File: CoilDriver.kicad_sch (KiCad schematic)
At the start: 27 parts, among them Q1 IRLML2803, Q2 SiRA99DP, U2 DRV8235RTER

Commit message: v3.1 Updates
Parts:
- removed R48, R50: 0R, Resistor_SMD:R_0603_1608Metric, symbol Device:R_Small
- C37: renamed from C26; value 10uF -> 10u; symbol Device:C -> Device:C_Small
- C38: renamed from C27; value 0.1uF -> 100n; symbol Device:C -> Device:C_Small
- C41: renamed from C22; value 1nF -> 1n; symbol Device:C -> Device:C_Small
- C42: renamed from C28; value 0.1uF -> 100n; symbol Device:C -> Device:C_Small
- R68: renamed from R33; symbol Device:R -> Device:R_Small
- R86: renamed from R49; now not fitted
- R87: renamed from R51; now not fitted
- R88: renamed from R32; symbol Device:R -> Device:R_Small
- R89: renamed from R52; symbol Device:R -> Device:R_Small
- R90: renamed from R53; symbol Device:R -> Device:R_Small
- renumbered F2 to F10, Q2 to Q16, Q1 to Q17, R36 to R64, R37 to R65, R39 to R66, R38 to R67, R54 to R69, R28 to R82, R29 to R83, R30 to R84, R31 to R85, U2 to U9
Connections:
- net PERI_3V3 is gone; now on net 3V3_P: R69.2
- net A0_COIL renamed A0
- net A1_COIL renamed A1
- net MAIN_3V3 renamed 3V3_P
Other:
- sheet I2C Single Protection renamed I2C Single Protection4
- sheet I2C Single Protection1 renamed I2C Single Protection5
- note added: "#TODO: Spec Resistors"
- company: (none) -> Carnegie Mellon University
- title: (none) -> Argus XY Solar Panel
- moved on the sheet: C37, C41, C42, D10, D9, F10, Q16, Q17, R64, R65, R66, R67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

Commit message: Local Stash
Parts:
- R64: value 2.7k -> 2k7
- R69: symbol SolarPanels:R_Small -> Device:R_Small
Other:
- moved on the sheet: C42, R66, R90
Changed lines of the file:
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@@
 	(wire
 		(pts
-			(xy 205.74 137.16) (xy 205.74 140.97)
+			(xy 205.74 137.16) (xy 205.74 139.7)
 		)
 		(stroke
@@
 	(wire
 		(pts
-			(xy 222.25 146.05) (xy 222.25 148.59)
+			(xy 222.25 144.78) (xy 222.25 147.32)
 		)
 		(stroke
@@
 	(wire
 		(pts
-			(xy 69.85 71.12) (xy 71.12 71.12)
+			(xy 68.58 71.12) (xy 71.12 71.12)
 		)
 		(stroke
@@
 	(wire
 		(pts
-			(xy 222.25 137.16) (xy 222.25 140.97)
+			(xy 222.25 137.16) (xy 222.25 139.7)
 		)
 		(stroke
@@
 	(wire
 		(pts
-			(xy 205.74 146.05) (xy 205.74 148.59)
+			(xy 205.74 144.78) (xy 205.74 147.32)
 		)
 		(stroke
@@
 	(wire
 		(pts
-			(xy 63.5 71.12) (xy 64.77 71.12)
-		)
-		(stroke
-			(width 0)
-			(type default)
-		)
-	)
-	(wire
-		(pts
 			(xy 124.46 82.55) (xy 124.46 81.28)
 		)
@@
 	)
 	(symbol
-		(lib_name "R_Small_1")
 		(lib_id "Device:R_Small")
 		(at 222.25 132.08 0)
@@
 			)
 		)
-		(property "Value" "2.7k"
+		(property "Value" "2k7"
 			(at 45.72 79.248 0)
 			(effects
@@
 	(symbol
 		(lib_id "Device:C_Small")
-		(at 205.74 143.51 0)
+		(at 205.74 142.24 0)
 		(unit 1)
 		(exclude_from_sim no)
@@
 		(dnp no)
 		(property "Reference" "C42"
-			(at 208.788 142.494 0)
+			(at 208.788 141.224 0)
 			(effects
 				(font
@@
 		)
 		(property "Value" "100n"
-			(at 208.788 144.526 0)
+			(at 208.788 143.256 0)
 			(effects
 				(font
@@
 		)
 		(property "Footprint" "Capacitor_SMD:C_0603_1608Metric"
-			(at 205.74 143.51 0)
+			(at 205.74 142.24 0)
 			(effects
 				(font
@@
 		)
 		(property "Datasheet" "~"
-			(at 205.74 143.51 0)
+			(at 205.74 142.24 0)
 			(effects
 				(font
@@
 		)
 		(property "Description" "Unpolarized capacitor, small symbol"
-			(at 205.74 143.51 0)
+			(at 205.74 142.24 0)
 			(effects
 				(font
@@
 	(symbol
 		(lib_id "power:GND")
-		(at 205.74 148.59 0)
+		(at 205.74 147.32 0)
 		(unit 1)
 		(exclude_from_sim no)
@@
 		(dnp no)
 		(property "Reference" "#PWR036"
-			(at 205.74 154.94 0)
+			(at 205.74 153.67 0)
 			(effects
 				(font
@@
 		)
 		(property "Value" "GND"
-			(at 205.74 152.654 0)
+			(at 205.74 151.384 0)
 			(effects
 				(font
@@
 		)
 		(property "Footprint" ""
-			(at 205.74 148.59 0)
+			(at 205.74 147.32 0)
 			(effects
 				(font
@@
 		)
 		(property "Datasheet" ""
-			(at 205.74 148.59 0)
+			(at 205.74 147.32 0)
 			(effects
 				(font
@@
 		)
 		(property "Description" "Power symbol creates a global label with name \"GND\" , ground"
-			(at 205.74 148.59 0)
+			(at 205.74 147.32 0)
 			(effects
 				(font
@@
 	)
 	(symbol
-		(lib_id "SolarPanels:R_Small")
+		(lib_id "Device:R_Small")
 		(at 241.3 81.28 180)
 		(unit 1)
@@
 	)
 	(symbol
-		(lib_name "R_Small_2")
 		(lib_id "Device:R_Small")
 		(at 149.86 73.66 0)
@@
 	(symbol
 		(lib_id "Device:R_Small")
-		(at 67.31 71.12 90)
+		(at 66.04 71.12 90)
 		(unit 1)
 		(exclude_from_sim no)
@@
 		(dnp no)
 		(property "Reference" "R66"
-			(at 67.31 73.406 90)
+			(at 66.04 73.406 90)
 			(effects
 				(font
@@
 		)
 		(property "Value" "4k7"
-			(at 67.056 75.438 90)
+			(at 65.786 75.438 90)
 			(effects
 				(font
@@
 		)
 		(property "Footprint" "Resistor_SMD:R_0603_1608Metric"
-			(at 67.31 71.12 0)
+			(at 66.04 71.12 0)
 			(effects
 				(font
@@
 		)
 		(property "Datasheet" "~"
-			(at 67.31 71.12 0)
+			(at 66.04 71.12 0)
 			(effects
 				(font
@@
 		)
 		(property "Description" "Resistor, small symbol"
-			(at 67.31 71.12 0)
+			(at 66.04 71.12 0)
 			(effects
 				(font
@@
 			)
 		)
+		(property "Sim.Pin" "1=K 2=A"
+			(at 46.99 85.09 0)
+			(effects
+				(font
+					(size 1.27 1.27)
+				)
+				(hide yes)
+			)
+		)
 		(pin "2"
 		)
@@
 	(symbol
 		(lib_id "power:GND")
-		(at 222.25 148.59 0)
+		(at 222.25 147.32 0)
 		(unit 1)
 		(exclude_from_sim no)
@@
 		(dnp no)
 		(property "Reference" "#PWR039"
-			(at 222.25 154.94 0)
+			(at 222.25 153.67 0)
 			(effects
 				(font
@@
 		)
 		(property "Value" "GND"
-			(at 222.25 152.654 0)
+			(at 222.25 151.384 0)
 			(effects
 				(font
@@
 		)
 		(property "Footprint" ""
-			(at 222.25 148.59 0)
+			(at 222.25 147.32 0)
 			(effects
 				(font
@@
 		)
 		(property "Datasheet" ""
-			(at 222.25 148.59 0)
+			(at 222.25 147.32 0)
 			(effects
 				(font
@@
 		)
 		(property "Description" "Power symbol creates a global label with name \"GND\" , ground"
-			(at 222.25 148.59 0)
+			(at 222.25 147.32 0)
 			(effects
 				(font
@@
 	)
 	(symbol
-		(lib_name "R_Small_3")
 		(lib_id "Device:R_Small")
-		(at 222.25 143.51 0)
+		(at 222.25 142.24 0)
 		(unit 1)
 		(exclude_from_sim no)
@@
 		(dnp no)
 		(property "Reference" "R90"
-			(at 223.774 142.494 0)
+			(at 223.774 141.224 0)
 			(effects
 				(font
@@
 		)
 		(property "Value" "TBD"
-			(at 223.774 144.526 0)
+			(at 223.774 143.256 0)
 			(effects
 				(font
@@
 		)
 		(property "Footprint" "Resistor_SMD:R_0603_1608Metric"
-			(at 222.25 143.51 0)
+			(at 222.25 142.24 0)
 			(effects
 				(font
@@
 		)
 		(property "Datasheet" "~"
-			(at 222.25 143.51 0)
+			(at 222.25 142.24 0)
 			(effects
 				(font
@@
 		)
 		(property "Description" "Resistor, small symbol"
-			(at 222.25 143.51 0)
+			(at 222.25 142.24 0)
 			(effects
 				(font
@@
 	)
 	(symbol
-		(lib_name "R_Small_4")
 		(lib_id "Device:R_Small")
 		(at 167.64 137.16 0)

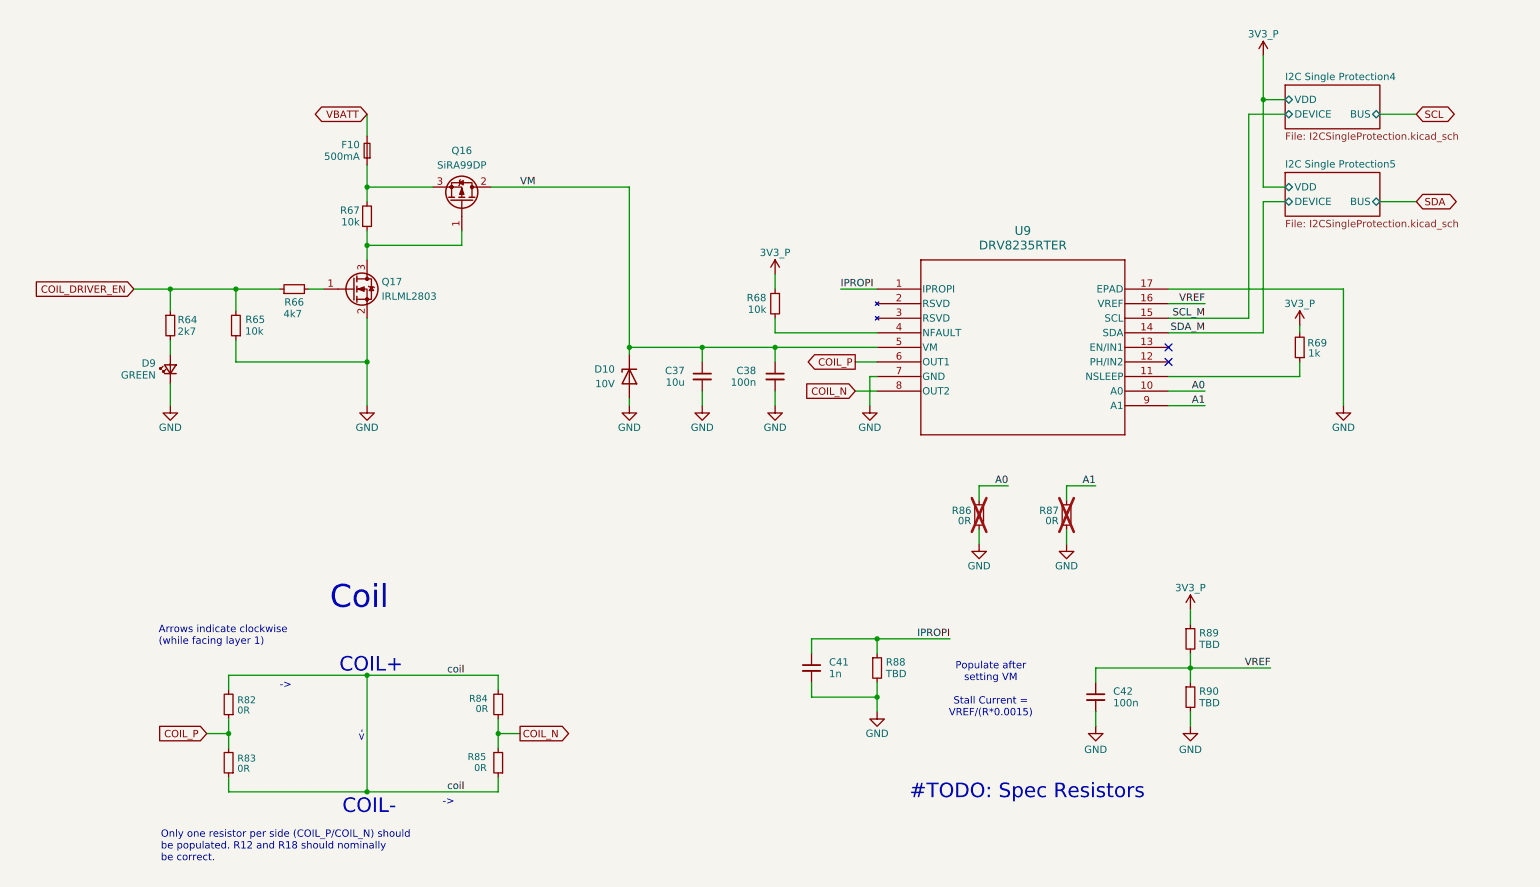
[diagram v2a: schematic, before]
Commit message: Updated access port, added deployment sensor
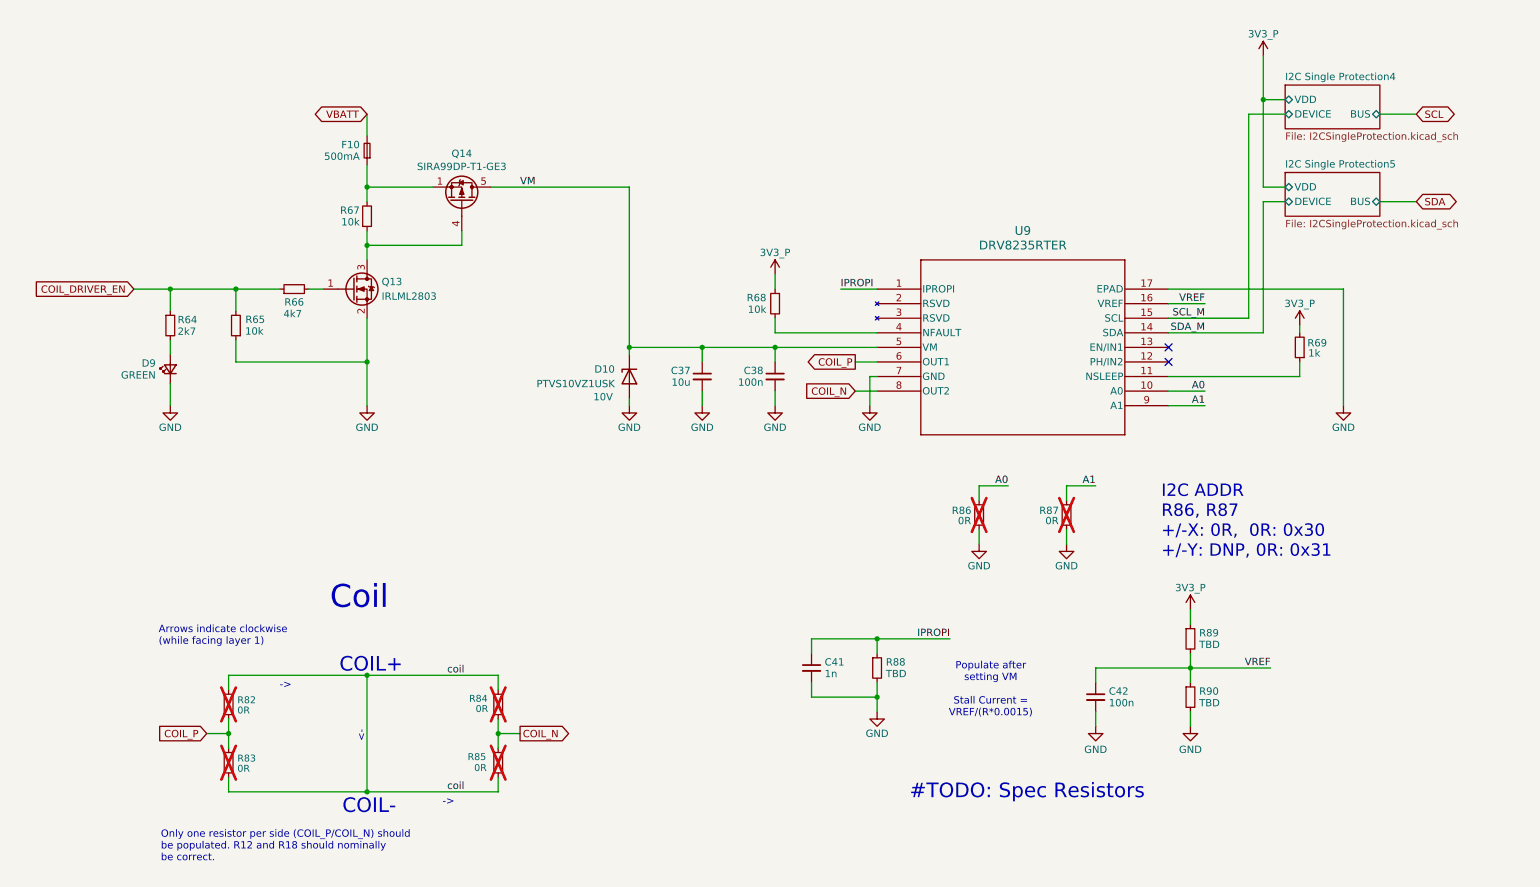
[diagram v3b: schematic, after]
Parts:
- removed Q16: SiRA99DP, Argus-Miscellaneous:PowerPAK SO-8, symbol Argus-IC:Q_PMOS_GDS
- added Q14: SIRA99DP-T1-GE3, Package_SO:PowerPAK_SO-8_Single, symbol Transistor_FET:Si7141DP
- C37: MPN (none) -> C126617
- C38, C42: MPN (none) -> C307348
- C41: MPN (none) -> C161231
- D10: value 10V -> PTVS10VZ1USK; Field5 (none) -> 10V
- D9: DIS Digi-Key -> (none); DPN 1830-1064-1-ND -> (none); MFR Inolux -> (none); MPN IN-S63AT5A -> C2909774
- Q13: renamed from Q17; MPN (none) -> C2590
- R64: DIS Digi-Key -> (none); DPN A129693CT-ND -> (none); MFR TE -> (none); MPN CRGCQ0603F2K7 -> C237112
- R65, R67: DIS Digi-Key -> (none); DPN 311-10.0KHRCT-ND -> (none); MFR Yageo -> (none); MPN RC0603FR-0710KL -> C2479067
- R66: MPN (none) -> C844931
- R68: MPN (none) -> C2479067
- R69: MPN (none) -> C2484712
- R82, R83, R84, R85: now not fitted; now left out of the parts list
- R86, R87: now left out of the parts list
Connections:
- net VM: now also Q14.5 (D)
- net at Q13.3 (D), R67.1: now also Q14.4 (G)
- net at F10.1, R67.2: now also Q14.1 (S), Q14.2 (S), Q14.3 (S)
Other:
- note added: "I2C ADDR R86, R87 +/-X: 0R, 0R: 0x30 +/-Y: DNP, 0R: 0x31"

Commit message: Local Stash
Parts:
- R82, R83, R84, R85: now fitted; now in the parts list
- R86, R87: value 0R -> ?R; now fitted; now in the parts list
- R88: value TBD -> 560R
- R89: value TBD -> 2k7
- R90: value TBD -> 1M
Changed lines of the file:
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@@
 			)
 		)
-		(property "Value" "TBD"
+		(property "Value" "2k7"
 			(at 223.774 133.096 0)
 			(effects
@@
 		(unit 1)
 		(exclude_from_sim no)
-		(in_bom no)
-		(on_board yes)
-		(dnp yes)
+		(in_bom yes)
+		(on_board yes)
+		(dnp no)
 		(property "Reference" "R87"
 			(at 197.612 109.728 0)
@@
 			)
 		)
-		(property "Value" "0R"
+		(property "Value" "?R"
 			(at 198.12 111.506 0)
 			(effects
@@
 		(unit 1)
 		(exclude_from_sim no)
-		(in_bom no)
-		(on_board yes)
-		(dnp yes)
+		(in_bom yes)
+		(on_board yes)
+		(dnp no)
 		(property "Reference" "R82"
 			(at 56.134 142.748 0)
@@
 		(unit 1)
 		(exclude_from_sim no)
-		(in_bom no)
-		(on_board yes)
-		(dnp yes)
+		(in_bom yes)
+		(on_board yes)
+		(dnp no)
 		(property "Reference" "R86"
 			(at 182.372 109.728 0)
@@
 			)
 		)
-		(property "Value" "0R"
+		(property "Value" "?R"
 			(at 182.88 111.506 0)
 			(effects
@@
 		(unit 1)
 		(exclude_from_sim no)
-		(in_bom no)
-		(on_board yes)
-		(dnp yes)
+		(in_bom yes)
+		(on_board yes)
+		(dnp no)
 		(property "Reference" "R84"
 			(at 96.52 142.494 0)
@@
 		(unit 1)
 		(exclude_from_sim no)
-		(in_bom no)
-		(on_board yes)
-		(dnp yes)
+		(in_bom yes)
+		(on_board yes)
+		(dnp no)
 		(property "Reference" "R83"
 			(at 56.134 152.908 0)
@@
 		(unit 1)
 		(exclude_from_sim no)
-		(in_bom no)
-		(on_board yes)
-		(dnp yes)
+		(in_bom yes)
+		(on_board yes)
+		(dnp no)
 		(property "Reference" "R85"
 			(at 96.266 152.654 0)
@@
 			)
 		)
-		(property "Value" "TBD"
+		(property "Value" "1M"
 			(at 223.774 143.256 0)
 			(effects
@@
 			)
 		)
-		(property "Value" "TBD"
+		(property "Value" "560R"
 			(at 169.164 138.176 0)
 			(effects

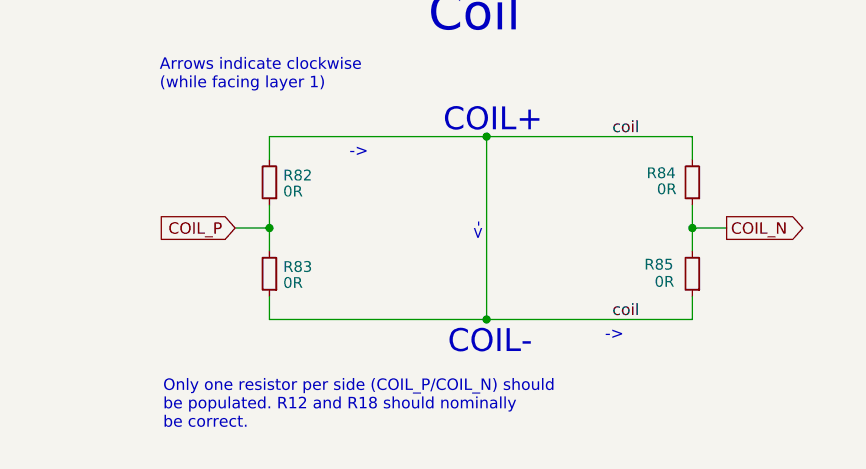
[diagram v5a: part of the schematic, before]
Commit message: Coil direction comment clarification
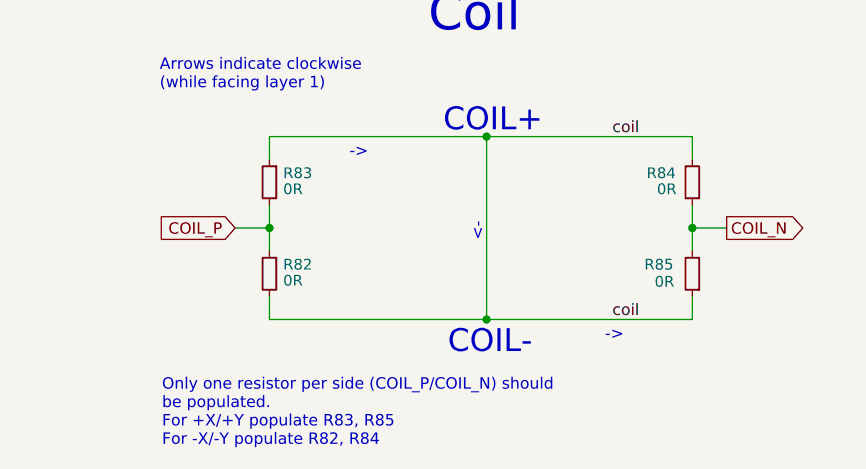
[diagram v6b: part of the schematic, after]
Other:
- note added: "Only one resistor per side (COIL_P/COIL_N) should be populated. For +X/+Y populate R83, R85 For -X/-Y populate R82, R84"
- note removed: "Only one resistor per side (COIL_P/COIL_N) should be populated. R12 and R18 should nominally be correct."
- moved on the sheet: R82, R83
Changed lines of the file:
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@@
 		)
 	)
-	(text "Only one resistor per side (COIL_P/COIL_N) should \nbe populated. R12 and R18 should nominally \nbe correct."
+	(text "Only one resistor per side (COIL_P/COIL_N) should \nbe populated.\nFor +X/+Y populate R83, R85\nFor -X/-Y populate R82, R84"
 		(exclude_from_sim no)
-		(at 42.799 171.069 0)
+		(at 42.672 172.974 0)
 		(effects
 			(font
@@
 	(symbol
 		(lib_id "Device:R_Small")
-		(at 54.61 143.51 180)
+		(at 54.61 153.67 0)
+		(mirror y)
 		(unit 1)
 		(exclude_from_sim no)
@@
 		(dnp no)
 		(property "Reference" "R82"
-			(at 56.134 142.748 0)
+			(at 56.134 152.654 0)
 			(effects
 				(font
@@
 		)
 		(property "Value" "0R"
-			(at 56.134 144.526 0)
+			(at 56.134 154.432 0)
 			(effects
 				(font
@@
 		)
 		(property "Footprint" "Resistor_SMD:R_0603_1608Metric"
-			(at 54.61 143.51 0)
+			(at 54.61 153.67 0)
 			(effects
 				(font
@@
 		)
 		(property "Datasheet" "~"
-			(at 54.61 143.51 0)
+			(at 54.61 153.67 0)
 			(effects
 				(font
@@
 		)
 		(property "Description" "Resistor, small symbol"
-			(at 54.61 143.51 0)
+			(at 54.61 153.67 0)
 			(effects
 				(font
@@
 		)
 		(instances
-			(project ""
+			(project "Avionics-SolarPanels"
 				(path "/92e58b76-9357-4452-b231-18fffdf58e73/757bbe31-359d-4282-a8be-b82658fcdbcd"
 					(reference "D10")
@@
 	(symbol
 		(lib_id "Device:R_Small")
-		(at 54.61 153.67 180)
+		(at 54.61 143.51 0)
+		(mirror y)
 		(unit 1)
 		(exclude_from_sim no)
@@
 		(dnp no)
 		(property "Reference" "R83"
-			(at 56.134 152.908 0)
+			(at 56.134 142.494 0)
 			(effects
 				(font
@@
 		)
 		(property "Value" "0R"
-			(at 56.134 154.686 0)
+			(at 56.134 144.272 0)
 			(effects
 				(font
@@
 		)
 		(property "Footprint" "Resistor_SMD:R_0603_1608Metric"
-			(at 54.61 153.67 0)
+			(at 54.61 143.51 0)
 			(effects
 				(font
@@
 		)
 		(property "Datasheet" "~"
-			(at 54.61 153.67 0)
+			(at 54.61 143.51 0)
 			(effects
 				(font
@@
 		)
 		(property "Description" "Resistor, small symbol"
-			(at 54.61 153.67 0)
+			(at 54.61 143.51 0)
 			(effects
 				(font
